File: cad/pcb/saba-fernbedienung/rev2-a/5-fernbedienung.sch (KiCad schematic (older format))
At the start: 49 parts, among them K601 G6K-2, K602 G6K-2, K603 G6K-2, K604 G6K-2, K605 G6K-2, K606 G6K-2, K607 EC2-5TNU, Q601 BC846, Q602 BC846, Q603 BC846, Q604 BC846, Q605 BC846, Q606 BC846, Q607 BC846, U601 LTV-357T

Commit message: ToDo-s bearbeitet
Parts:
- removed K607: EC2-5TNU, Relay_THT:Relay_DPDT_Kemet_EC2_DoubleCoil, symbol Relay:EC2-5TNU
- added D? (x2): SMAJ33CA, Diode_SMD:D_SMA, symbol Device:D_TVS
- added K?: RT42xFxx, Relay_THT:Relay_DPDT_Schrack-RT2-FormC-Dual-Coil_RM5mm, symbol Relay:RT42xFxx
- added Q?: BC846, Package_TO_SOT_SMD:SOT-23, symbol Transistor_BJT:BC846
- added R? (x2): 4k7, Resistor_SMD:R_0603_1608Metric, symbol Device:R
- added R?: 10k, Resistor_SMD:R_0603_1608Metric, symbol Device:R
- R601, R602, R607, R608, R613, R614, R619, R622: value 1k -> 4k7
- R604, R605, R610, R611, R615, R616, R623: value 100k -> 4k7
- R618: value 5k7 -> 5k6
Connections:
- net +3V3: now also R?.1
- net +5V: now also D607.1 (K), D608.1 (K), K?.A3
- net GND: now also K?.14, Q?.2 (E), R?.1
- net Relais_Laut: now also K601.2, Q604.3 (C); no longer K603.2, Q602.3 (C)
- net Relais_Leise: now also K603.2, Q602.3 (C); no longer K601.2, Q604.3 (C)
- net Relais_Suchlauf_L: now also D601.2 (A), K602.8, Q601.3 (C); no longer D606.2 (A), K605.8, Q603.3 (C)
- net Relais_Suchlauf_R: now also D606.2 (A), K605.8, Q603.3 (C); no longer D601.2 (A), K602.8, Q601.3 (C)
- net SABA_15V_AC: now also D?.2 (A2)
- net SABA_230V_AC: now also K?.21
- net SABA_Laut: now also R608.2; no longer R602.2
- net SABA_Lautstaerke: now also D?.1 (A1), D?.2 (A2)
- net SABA_Leise: now also R602.2; no longer R608.2
- net SABA_N1: now also K?.22
- net SABA_N2: now also K?.24
- net SABA_Suchlauf_L: now also R601.2; no longer R607.2
- net SABA_Suchlauf_R: now also R607.2; no longer R601.2
- net SABA_~15V_AC: now also D?.1 (A1)
- net at D608.2 (A), Q607.3 (C): now also K?.A2; no longer D607.2 (A)
- net SABA_Netz renamed SABA_Netz_Reset
- new net: D607.2 (A), K?.A1, Q?.3 (C)
- new net: Q?.1 (B), R?.1, R?.2
- new net SABA_Netz_Feedback: K?.11, R?.2
- new net SABA_Netz_Set: R?.2
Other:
- note removed: "ToDo - Widerstandswerte abgleichen \nso dass Verhalten wie mit Haltespule ist"
- moved on the sheet: D607, D608, Q607, R622, R623

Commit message: Change: Bauteilbezeichner
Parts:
- gave numbers to parts that had none: 7
- renumbered D602 to D603, D603 to D604, D604 to D606, D605 to D607, D606 to D608, D607 to D609, D608 to D610, D609 to D611, D610 to D612, Q607 to Q608, R622 to R623, R623 to R626
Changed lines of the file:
@@
 $EndComp
 $Comp
-L Device:D D606
+L Device:D D608
 U 1 1 600555C5
 P 2400 4800
-F 0 "D606" H 2400 5017 50  0000 C CNN
+F 0 "D608" H 2400 5017 50  0000 C CNN
 F 1 "1N4148" H 2400 4926 50  0000 C CNN
 F 2 "Diode_SMD:D_SOD-323F" H 2400 4800 50  0001 C CNN
@@
 $EndComp
 $Comp
-L Device:D D603
+L Device:D D604
 U 1 1 60057103
 P 3550 1950
-F 0 "D603" H 3550 2167 50  0000 C CNN
+F 0 "D604" H 3550 2167 50  0000 C CNN
 F 1 "1N4148" H 3550 2076 50  0000 C CNN
 F 2 "Diode_SMD:D_SOD-323F" H 3550 1950 50  0001 C CNN
@@
 P 2700 5650
 AR Path="/60135668/60147585" Ref="#PWR?"  Part="1"
-AR Path="/6044FE50/60147585" Ref="#PWR0613"  Part="1"
-F 0 "#PWR0613" H 2700 5500 50  0001 C CNN
+AR Path="/6044FE50/60147585" Ref="#PWR0614"  Part="1"
+F 0 "#PWR0614" H 2700 5500 50  0001 C CNN
 F 1 "+3.3V" H 2715 5823 50  0000 C CNN
 F 2 "" H 2700 5650 50  0001 C CNN
@@
 P 2550 6750
 AR Path="/60135668/6014758B" Ref="#PWR?"  Part="1"
-AR Path="/6044FE50/6014758B" Ref="#PWR0615"  Part="1"
-F 0 "#PWR0615" H 2550 6500 50  0001 C CNN
+AR Path="/6044FE50/6014758B" Ref="#PWR0616"  Part="1"
+F 0 "#PWR0616" H 2550 6500 50  0001 C CNN
 F 1 "GND" H 2555 6577 50  0000 C CNN
 F 2 "" H 2550 6750 50  0001 C CNN
@@
 P 3250 6750
 AR Path="/60135668/6014759D" Ref="#PWR?"  Part="1"
-AR Path="/6044FE50/6014759D" Ref="#PWR0616"  Part="1"
-F 0 "#PWR0616" H 3250 6500 50  0001 C CNN
+AR Path="/6044FE50/6014759D" Ref="#PWR0617"  Part="1"
+F 0 "#PWR0617" H 3250 6500 50  0001 C CNN
 F 1 "GND" H 3255 6577 50  0000 C CNN
 F 2 "" H 3250 6750 50  0001 C CNN
@@
 AR Path="/5FFC49DA/601475C0" Ref="D?"  Part="1"
 AR Path="/60135668/601475C0" Ref="D?"  Part="1"
-AR Path="/6044FE50/601475C0" Ref="D610"  Part="1"
-F 0 "D610" V 1939 6532 50  0000 R CNN
+AR Path="/6044FE50/601475C0" Ref="D612"  Part="1"
+F 0 "D612" V 1939 6532 50  0000 R CNN
 F 1 "LED" V 1848 6532 50  0000 R CNN
 F 2 "LED_SMD:LED_0805_2012Metric" H 1900 6650 50  0001 C CNN
@@
 	1900 6450 1900 6500
 $Comp
-L Device:D D609
+L Device:D D611
 U 1 1 6014EEE0
 P 1250 6600
-F 0 "D609" V 1200 6950 50  0000 R CNN
+F 0 "D611" V 1200 6950 50  0000 R CNN
 F 1 "1N4148" V 1300 7000 50  0000 R CNN
 F 2 "Diode_SMD:D_SOD-323F" H 1250 6600 50  0001 C CNN
@@
 	7100 2900 7200 2900
 $Comp
-L Device:D D602
+L Device:D D603
 U 1 1 60233DE2
 P 9000 1500
-F 0 "D602" V 8954 1420 50  0000 R CNN
+F 0 "D603" V 8954 1420 50  0000 R CNN
 F 1 "1N4148" V 9045 1420 50  0000 R CNN
 F 2 "Diode_SMD:D_SOD-323F" H 9000 1500 50  0001 C CNN
@@
 $EndComp
 $Comp
-L Device:D D605
+L Device:D D607
 U 1 1 6026B529
 P 9000 3900
-F 0 "D605" V 9046 3980 50  0000 L CNN
+F 0 "D607" V 9046 3980 50  0000 L CNN
 F 1 "1N4148" V 8955 3980 50  0000 L CNN
 F 2 "Diode_SMD:D_SOD-323F" H 9000 3900 50  0001 C CNN
@@
 P 6100 7250
 AR Path="/60135668/6031DB0D" Ref="#PWR?"  Part="1"
-AR Path="/6044FE50/6031DB0D" Ref="#PWR0617"  Part="1"
-F 0 "#PWR0617" H 6100 7000 50  0001 C CNN
+AR Path="/6044FE50/6031DB0D" Ref="#PWR0620"  Part="1"
+F 0 "#PWR0620" H 6100 7000 50  0001 C CNN
 F 1 "GND" H 6105 7077 50  0000 C CNN
 F 2 "" H 6100 7250 50  0001 C CNN
@@
 AR Path="/6002EA57/6031DB14" Ref="R?"  Part="1"
 AR Path="/60135668/6031DB14" Ref="R?"  Part="1"
-AR Path="/6044FE50/6031DB14" Ref="R623"  Part="1"
-F 0 "R623" H 5680 6909 50  0000 R CNN
+AR Path="/6044FE50/6031DB14" Ref="R626"  Part="1"
+F 0 "R626" H 5680 6909 50  0000 R CNN
 F 1 "4k7" H 5680 7000 50  0000 R CNN
 F 2 "Resistor_SMD:R_0603_1608Metric" V 5680 7000 50  0001 C CNN
@@
 AR Path="/6002EA57/6031DB25" Ref="R?"  Part="1"
 AR Path="/60135668/6031DB25" Ref="R?"  Part="1"
-AR Path="/6044FE50/6031DB25" Ref="R622"  Part="1"
-F 0 "R622" H 5480 6659 50  0000 R CNN
+AR Path="/6044FE50/6031DB25" Ref="R623"  Part="1"
+F 0 "R623" H 5480 6659 50  0000 R CNN
 F 1 "4k7" H 5480 6750 50  0000 R CNN
 F 2 "Resistor_SMD:R_0603_1608Metric" V 5480 6750 50  0001 C CNN
@@
 SABA_N2
 $Comp
-L Device:D D607
+L Device:D D609
 U 1 1 6035A1FC
 P 5550 5700
-F 0 "D607" V 5550 5550 50  0000 R CNN
+F 0 "D609" V 5550 5550 50  0000 R CNN
 F 1 "1N4148" V 5450 5600 50  0000 R CNN
 F 2 "Diode_SMD:D_SOD-323F" H 5550 5700 50  0001 C CNN
@@
 $EndComp
 $Comp
-L Device:D D608
+L Device:D D610
 U 1 1 6035AC20
 P 5550 6200
-F 0 "D608" V 5550 6550 50  0000 R CNN
+F 0 "D610" V 5550 6550 50  0000 R CNN
 F 1 "1N4148" V 5650 6600 50  0000 R CNN
 F 2 "Diode_SMD:D_SOD-323F" H 5550 6200 50  0001 C CNN
@@
 $EndComp
 $Comp
-L power:+5V #PWR0614
+L power:+5V #PWR0615
 U 1 1 603CB20D
 P 5900 5850
-F 0 "#PWR0614" H 5900 5700 50  0001 C CNN
+F 0 "#PWR0615" H 5900 5700 50  0001 C CNN
 F 1 "+5V" H 5915 6023 50  0000 C CNN
 F 2 "" H 5900 5850 50  0001 C CNN
@@
 $EndComp
 $Comp
-L Transistor_BJT:BC846 Q607
+L Transistor_BJT:BC846 Q608
 U 1 1 60015199
 P 6000 6750
-F 0 "Q607" H 5850 7000 50  0000 L CNN
+F 0 "Q608" H 5850 7000 50  0000 L CNN
 F 1 "BC846" H 5800 6900 50  0000 L CNN
 F 2 "Package_TO_SOT_SMD:SOT-23" H 6200 6675 50  0001 L CIN
@@
 $EndComp
 $Comp
-L Device:D D604
+L Device:D D606
 U 1 1 60234C49
 P 9000 2500
-F 0 "D604" V 9046 2580 50  0000 L CNN
+F 0 "D606" V 9046 2580 50  0000 L CNN
 F 1 "1N4148" V 8955 2580 50  0000 L CNN
 F 2 "Diode_SMD:D_SOD-323F" H 9000 2500 50  0001 C CNN
@@
 P 7200 1500
 AR Path="/60135668/614FD644" Ref="D?"  Part="1"
-AR Path="/6044FE50/614FD644" Ref="D?"  Part="1"
-F 0 "D?" V 7154 1580 50  0000 L CNN
+AR Path="/6044FE50/614FD644" Ref="D602"  Part="1"
+F 0 "D602" V 7154 1580 50  0000 L CNN
 F 1 "SMAJ33CA" V 7245 1580 50  0000 L CNN
 F 2 "Diode_SMD:D_SMA" H 7200 1500 50  0001 C CNN
@@
 P 7200 2500
 AR Path="/60135668/61509236" Ref="D?"  Part="1"
-AR Path="/6044FE50/61509236" Ref="D?"  Part="1"
-F 0 "D?" V 7154 2580 50  0000 L CNN
+AR Path="/6044FE50/61509236" Ref="D605"  Part="1"
+F 0 "D605" V 7154 2580 50  0000 L CNN
 F 1 "SMAJ33CA" V 7245 2580 50  0000 L CNN
 F 2 "Diode_SMD:D_SMA" H 7200 2500 50  0001 C CNN
@@
 	7200 2900 7450 2900
 $Comp
-L Relay:RT42xFxx K?
+L Relay:RT42xFxx K607
 U 1 1 61579A80
 P 6700 5950
-F 0 "K?" H 7330 6041 50  0000 L CNN
+F 0 "K607" H 7330 6041 50  0000 L CNN
 F 1 "RT42xFxx" H 7330 5950 50  0000 L CNN
 F 2 "Relay_THT:Relay_DPDT_Schrack-RT2-FormC-Dual-Coil_RM5mm" H 6700 5950 50  0001 C CNN
@@
 P 5050 7250
 AR Path="/60135668/616050CA" Ref="#PWR?"  Part="1"
-AR Path="/6044FE50/616050CA" Ref="#PWR?"  Part="1"
-F 0 "#PWR?" H 5050 7000 50  0001 C CNN
+AR Path="/6044FE50/616050CA" Ref="#PWR0619"  Part="1"
+F 0 "#PWR0619" H 5050 7000 50  0001 C CNN
 F 1 "GND" H 5055 7077 50  0000 C CNN
 F 2 "" H 5050 7250 50  0001 C CNN
@@
 AR Path="/6002EA57/616050D1" Ref="R?"  Part="1"
 AR Path="/60135668/616050D1" Ref="R?"  Part="1"
-AR Path="/6044FE50/616050D1" Ref="R?"  Part="1"
-F 0 "R?" H 4630 6909 50  0000 R CNN
+AR Path="/6044FE50/616050D1" Ref="R625"  Part="1"
+F 0 "R625" H 4630 6909 50  0000 R CNN
 F 1 "4k7" H 4630 7000 50  0000 R CNN
 F 2 "Resistor_SMD:R_0603_1608Metric" V 4630 7000 50  0001 C CNN
@@
 AR Path="/6002EA57/616050E1" Ref="R?"  Part="1"
 AR Path="/60135668/616050E1" Ref="R?"  Part="1"
-AR Path="/6044FE50/616050E1" Ref="R?"  Part="1"
-F 0 "R?" H 4430 6659 50  0000 R CNN
+AR Path="/6044FE50/616050E1" Ref="R622"  Part="1"
+F 0 "R622" H 4430 6659 50  0000 R CNN
 F 1 "4k7" H 4430 6750 50  0000 R CNN
 F 2 "Resistor_SMD:R_0603_1608Metric" V 4430 6750 50  0001 C CNN
@@
 $EndComp
 $Comp
-L Transistor_BJT:BC846 Q?
+L Transistor_BJT:BC846 Q607
 U 1 1 616050E8
 P 4950 6750
-F 0 "Q?" H 4750 7000 50  0000 L CNN
+F 0 "Q607" H 4750 7000 50  0000 L CNN
 F 1 "BC846" H 4750 6900 50  0000 L CNN
 F 2 "Package_TO_SOT_SMD:SOT-23" H 5150 6675 50  0001 L CIN
@@
 P 6800 5600
 AR Path="/60135668/616650C6" Ref="#PWR?"  Part="1"
-AR Path="/6044FE50/616650C6" Ref="#PWR?"  Part="1"
-F 0 "#PWR?" H 6800 5350 50  0001 C CNN
+AR Path="/6044FE50/616650C6" Ref="#PWR0613"  Part="1"
+F 0 "#PWR0613" H 6800 5350 50  0001 C CNN
 F 1 "GND" H 6805 5427 50  0000 C CNN
 F 2 "" H 6800 5600 50  0001 C CNN
@@
 AR Path="/6002EA57/616EBB99" Ref="R?"  Part="1"
 AR Path="/60135668/616EBB99" Ref="R?"  Part="1"
-AR Path="/6044FE50/616EBB99" Ref="R?"  Part="1"
-F 0 "R?" H 6330 6759 50  0000 R CNN
+AR Path="/6044FE50/616EBB99" Ref="R624"  Part="1"
+F 0 "R624" H 6330 6759 50  0000 R CNN
 F 1 "10k" H 6330 6850 50  0000 R CNN
 F 2 "Resistor_SMD:R_0603_1608Metric" V 6330 6850 50  0001 C CNN
@@
 P 6400 7150
 AR Path="/60135668/61764248" Ref="#PWR?"  Part="1"
-AR Path="/6044FE50/61764248" Ref="#PWR?"  Part="1"
-F 0 "#PWR?" H 6400 7000 50  0001 C CNN
+AR Path="/6044FE50/61764248" Ref="#PWR0618"  Part="1"
+F 0 "#PWR0618" H 6400 7000 50  0001 C CNN
 F 1 "+3.3V" H 6415 7323 50  0000 C CNN
 F 2 "" H 6400 7150 50  0001 C CNN

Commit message: Sicherung
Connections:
- net SABA_N1: now also K607.24; no longer K607.22
- net SABA_N2: now also K607.22; no longer K607.24
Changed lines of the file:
@@
 Text GLabel 7150 6350 2    50   Input ~ 0
 SABA_230V_AC
+Text GLabel 7300 5550 2    50   Output ~ 0
+SABA_N1
 Text GLabel 7300 5400 2    50   Output ~ 0
-SABA_N1
-Text GLabel 7300 5550 2    50   Output ~ 0
 SABA_N2
 $Comp

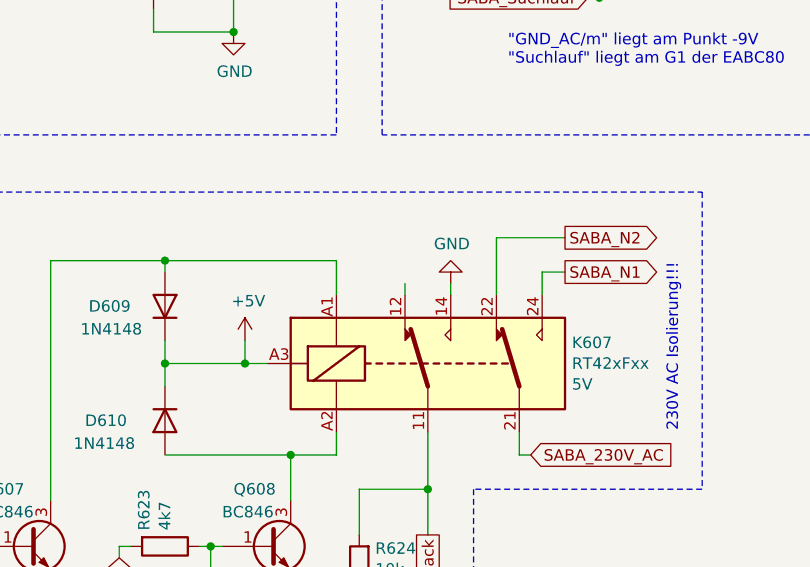
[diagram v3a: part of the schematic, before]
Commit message: alle Bauteile platziert
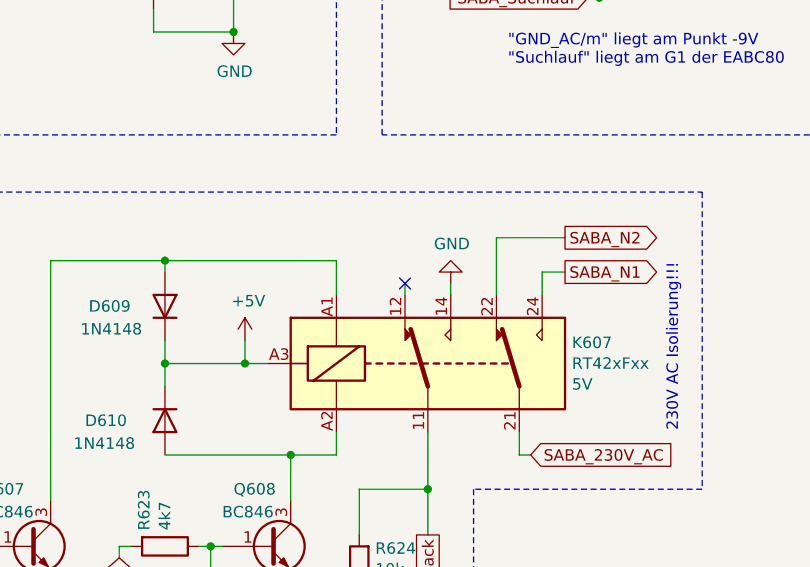
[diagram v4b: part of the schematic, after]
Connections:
- no-connect marks 12 -> 13
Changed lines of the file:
@@
 Wire Wire Line
 	6400 7000 6400 7150
+NoConn ~ 6600 5600
 $EndSCHEMATC

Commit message: Update NP, Fix ToDo-s
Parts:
- D609, D610, Q607, Q608, R622, R623, R624, R625, R626: Placement (none) -> NP
- K607: value RT42xFxx -> RT424F05; Alternative (none) -> rt424f06 (5V noch in der Toleranz der Spule); Placement (none) -> NP
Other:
- note added: "Netzschalter (Optional)"
- note removed: "Netzschalter"
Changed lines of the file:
@@
 Sheet 6 7
 Title "Fernbedienung - Webradio SABA 6-3D"
-Date "2021-08-14"
+Date "2022-06-05"
 Rev "2-A"
 Comp "Martin Wagner DL2WAG"
@@
 F 2 "Resistor_SMD:R_0603_1608Metric" V 5680 7000 50  0001 C CNN
 F 3 "~" H 5750 7000 50  0001 C CNN
-F 4 "" V 5750 7050 50  0000 R CNN "Placement"
+F 4 "NP" V 5750 7050 50  0000 R CNN "Placement"
 	1    5750 7000
 	-1   0    0    1
@@
 F 2 "Resistor_SMD:R_0603_1608Metric" V 5480 6750 50  0001 C CNN
 F 3 "~" H 5550 6750 50  0001 C CNN
-F 4 "" V 5550 6800 50  0000 R CNN "Placement"
+F 4 "NP" V 5550 6800 50  0000 R CNN "Placement"
 	1    5550 6750
 	0    1    1    0
@@
 F 3 "~" H 5550 5700 50  0001 C CNN
 F 4 "ON 1N4148WS" V 5550 5700 50  0001 C CNN "Bauteil"
+F 5 "NP" V 5550 5800 50  0000 C CNN "Placement"
 	1    5550 5700
 	0    1    -1   0
@@
 F 3 "~" H 5550 6200 50  0001 C CNN
 F 4 "ON 1N4148WS" V 5550 6200 50  0001 C CNN "Bauteil"
+F 5 "NP" V 5550 6100 50  0000 C CNN "Placement"
 	1    5550 6200
 	0    -1   1    0
@@
 	4100 7650 4100 5200
 Text Notes 4100 5150 0    79   ~ 0
-Netzschalter
+Netzschalter (Optional)
 NoConn ~ 7650 2800
 NoConn ~ 7850 2800
@@
 F 3 "" H 6000 6750 50  0001 L CNN
 F 4 "ON BC846BLT3G" H 6000 6750 50  0001 C CNN "Bauteil"
+F 5 "NP" H 5850 6800 50  0000 C CNN "Placement"
 	1    6000 6750
 	1    0    0    -1
@@
 P 6700 5950
 F 0 "K607" H 7330 6041 50  0000 L CNN
-F 1 "RT42xFxx" H 7330 5950 50  0000 L CNN
+F 1 "RT424F05" H 7330 5950 50  0000 L CNN
 F 2 "Relay_THT:Relay_DPDT_Schrack-RT2-FormC-Dual-Coil_RM5mm" H 6700 5950 50  0001 C CNN
 F 3 "http://www.te.com/commerce/DocumentDelivery/DDEController?Action=showdoc&DocId=Data+Sheet%7FRT2_bistable%7F1116%7Fpdf%7FEnglish%7FENG_DS_RT2_bistable_1116.pdf%7F1-1415537-8" H 6700 5950 50  0001 C CNN
 F 4 "5V" H 7330 5859 50  0000 L CNN "Coil Voltage"
+F 5 "NP" H 7400 5750 50  0000 C CNN "Placement"
+F 6 "rt424f06 (5V noch in der Toleranz der Spule)" H 6700 5950 50  0001 C CNN "Alternative"
 	1    6700 5950
 	1    0    0    -1
@@
 F 2 "Resistor_SMD:R_0603_1608Metric" V 4630 7000 50  0001 C CNN
 F 3 "~" H 4700 7000 50  0001 C CNN
-F 4 "" V 4700 7050 50  0000 R CNN "Placement"
+F 4 "NP" V 4700 7050 50  0000 R CNN "Placement"
 	1    4700 7000
 	-1   0    0    1
@@
 F 2 "Resistor_SMD:R_0603_1608Metric" V 4430 6750 50  0001 C CNN
 F 3 "~" H 4500 6750 50  0001 C CNN
-F 4 "" V 4500 6800 50  0000 R CNN "Placement"
+F 4 "NP" V 4500 6800 50  0000 R CNN "Placement"
 	1    4500 6750
 	0    1    1    0
@@
 F 3 "" H 4950 6750 50  0001 L CNN
 F 4 "ON BC846BLT3G" H 4950 6750 50  0001 C CNN "Bauteil"
+F 5 "NP" H 4800 6800 50  0000 C CNN "Placement"
 	1    4950 6750
 	1    0    0    -1
@@
 F 2 "Resistor_SMD:R_0603_1608Metric" V 6330 6850 50  0001 C CNN
 F 3 "~" H 6400 6850 50  0001 C CNN
-F 4 "" V 6400 6900 50  0000 R CNN "Placement"
+F 4 "NP" V 6400 6900 50  0000 R CNN "Placement"
 	1    6400 6850
 	-1   0    0    1
